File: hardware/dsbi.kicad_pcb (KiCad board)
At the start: 2 copper layers, 20 parts, among them U1 TL082, U2 TL082

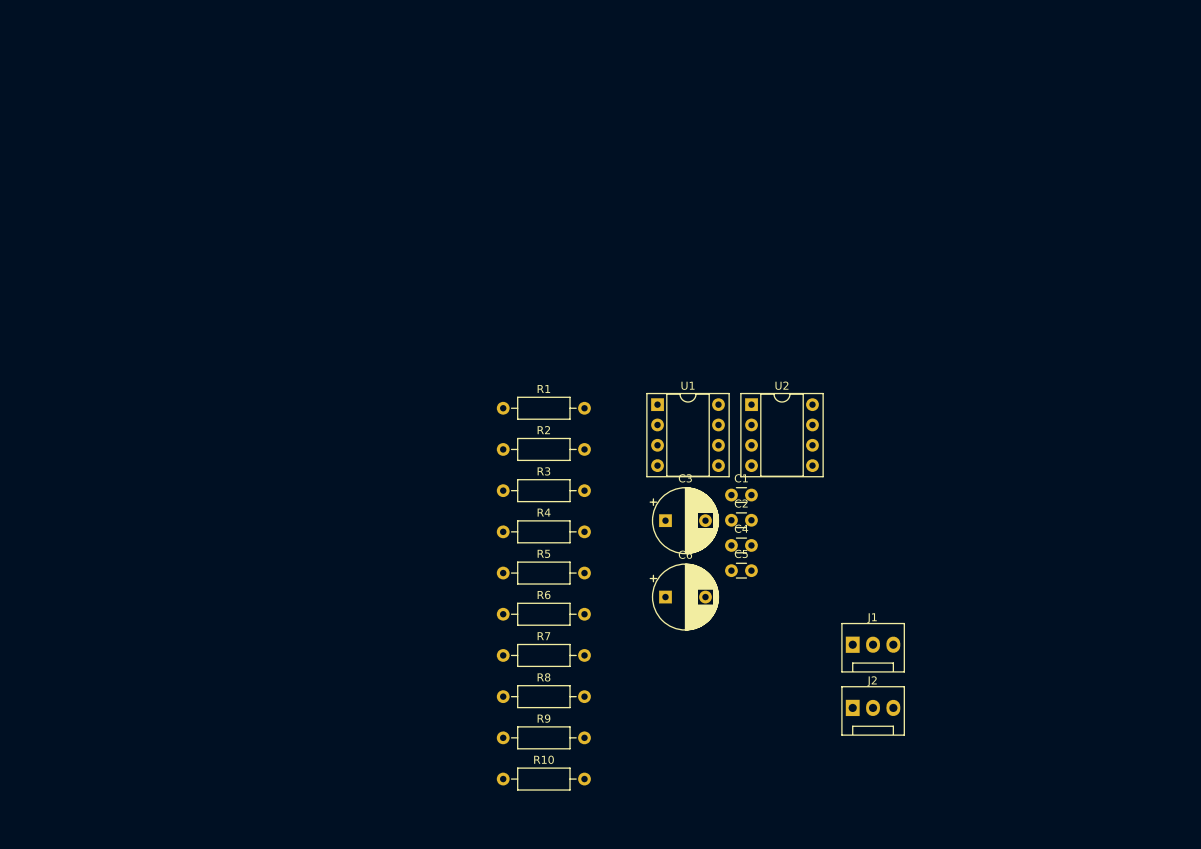
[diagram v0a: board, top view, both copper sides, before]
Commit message: Initial create circuits (#1)
* Arrangement of elements

* paths

* Do not track production files

* Most paths

* Rearrange elements

* Create new PCB paths

* Add footprints

* Create ESP32 adapter

* Add custom footprints (lib)

* Finish analog part
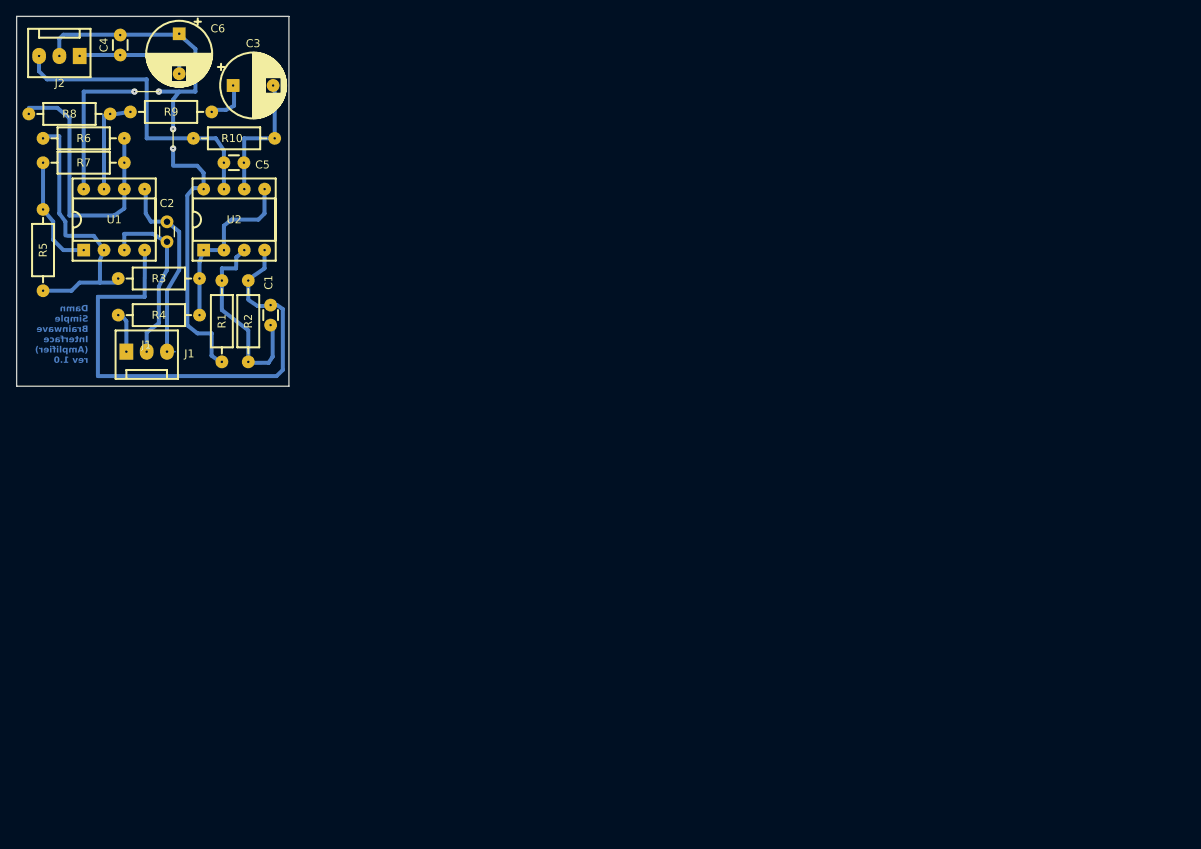
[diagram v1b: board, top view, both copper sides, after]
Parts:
- moved J2 126.4 mm to (20.2, 17.3), turned to 180 degrees
- moved C4 98.0 mm to (25.3, 17.2), turned to 90 degrees
- moved J1 97.9 mm to (26.0, 54.3)
- moved R8 93.9 mm to (13.9, 24.6)
- moved C6 93.0 mm to (32.6, 14.5), turned to -90 degrees
- moved R9 91.1 mm to (26.6, 24.3)
- moved R10 85.0 mm to (44.6, 27.6), turned to 180 degrees
- moved R7 84.3 mm to (15.6, 30.7)
- moved R6 82.8 mm to (15.6, 27.6)
- moved C5 79.5 mm to (40.7, 30.7), turned to 180 degrees
- moved C2 78.7 mm to (31.1, 40.5), turned to 90 degrees
- moved C3 76.7 mm to (39.4, 21.0)
- moved U1 74.3 mm to (20.7, 41.6), turned to 90 degrees
- moved U2 71.2 mm to (35.7, 41.6), turned to 90 degrees
- moved R5 67.5 mm to (15.6, 46.7), turned to 90 degrees
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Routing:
- net (no net): vias 0 -> 4
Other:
- board outline added: 34 x 46.2 mm
- board text added: "Damn Simple Brainwave Interface (Amplifier) rev 1.0"

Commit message: Improvements
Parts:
- moved C5 125.1 mm to (152.7, 86.5)
- moved J2 125.1 mm to (132.2, 73.1)
- moved R3 125.1 mm to (147.2, 101.0)
- moved R4 125.1 mm to (147.2, 105.5)
- moved U2 125.1 mm to (147.7, 97.4)
- moved C1 125.1 mm to (156.1, 104.3)
- moved C2 125.1 mm to (143.1, 96.4)
- moved C3 125.1 mm to (151.4, 76.8)
- moved C4 125.1 mm to (137.3, 73.0)
- moved C6 125.1 mm to (144.7, 70.4)
- moved J1 125.1 mm to (138.0, 110.1)
- moved R1 125.1 mm to (150.0, 101.2)
- moved R10 125.1 mm to (156.6, 83.4)
- moved R5 125.1 mm to (127.6, 102.5)
- moved R6 125.1 mm to (127.6, 83.4)
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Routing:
- net (no net): vias 4 -> 6
